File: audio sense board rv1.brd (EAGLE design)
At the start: 127 x 26.7 mm, 33 parts, among them IC2 TSOP38238, J1 PJRAN1X1U01X, J2 PJRAN1X1U01X, Q1 2N3904, Q2 2N3904

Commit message: update lable positions
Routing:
- net IRREC: track 31.3 -> 29.8 mm
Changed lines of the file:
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@@
 <plain>
 <text x="46.228" y="21.717" size="1.397" layer="21" rot="R90">Ch2</text>
-<text x="13.335" y="22.225" size="1.397" layer="21" rot="R270">Ch1</text>
+<text x="14.605" y="20.955" size="1.397" layer="21" rot="R180">Ch1</text>
 <text x="100.33" y="3.048" size="1.016" layer="25">https://github.com/txoof/audioSensor</text>
 <wire x1="0" y1="-1.27" x2="0" y2="25.4" width="0.000253125" layer="20"/>
@@
 </element>
 <element name="IR_LED" library="SparkFun-Connectors" library_urn="urn:adsk.eagle:library:513" package="1X02_LOCK" package3d_urn="urn:adsk.eagle:package:38045/1" value="IR LED connection" x="109.22" y="20.32" smashed="yes" rot="R180">
-<attribute name="NAME" x="114.3" y="18.923" size="0.8128" layer="25" font="vector" ratio="20" rot="R180"/>
+<attribute name="NAME" x="109.22" y="22.733" size="0.8128" layer="25" font="vector" ratio="20" rot="R180"/>
 <attribute name="VALUE" x="110.49" y="22.352" size="0.6096" layer="27" font="vector" ratio="20" rot="R180"/>
 </element>
@@
 </element>
 <element name="DEBUG" library="SparkFun-Connectors" library_urn="urn:adsk.eagle:library:513" package="1X02_LOCK" package3d_urn="urn:adsk.eagle:package:38045/1" value="Debug Jumper" x="121.92" y="20.32" smashed="yes" rot="R180">
-<attribute name="NAME" x="123.19" y="17.907" size="0.8128" layer="25" font="vector" ratio="20"/>
+<attribute name="NAME" x="118.11" y="21.717" size="0.8128" layer="25" font="vector" ratio="20"/>
 <attribute name="VALUE" x="123.19" y="22.352" size="0.6096" layer="27" font="vector" ratio="20" rot="R180"/>
 </element>
@@
 <wire x1="101.6" y1="23.495" x2="101.6" y2="21.77" width="0.3048" layer="16"/>
 <wire x1="123.19" y1="23.495" x2="101.6" y2="23.495" width="0.3048" layer="16"/>
-<wire x1="124.46" y1="22.225" x2="123.19" y2="23.495" width="0.3048" layer="16"/>
-<wire x1="124.46" y1="17.78" x2="124.46" y2="22.225" width="0.3048" layer="16"/>
-<wire x1="123.825" y1="17.145" x2="124.46" y2="17.78" width="0.3048" layer="16"/>
-<wire x1="123.19" y1="17.145" x2="123.825" y2="17.145" width="0.3048" layer="16"/>
-<wire x1="123.19" y1="17.145" x2="123.19" y2="16.97" width="0.3048" layer="16"/>
+<wire x1="123.19" y1="16.97" x2="123.19" y2="23.495" width="0.3048" layer="16"/>
 </signal>
 <signal name="DEBUGJ">

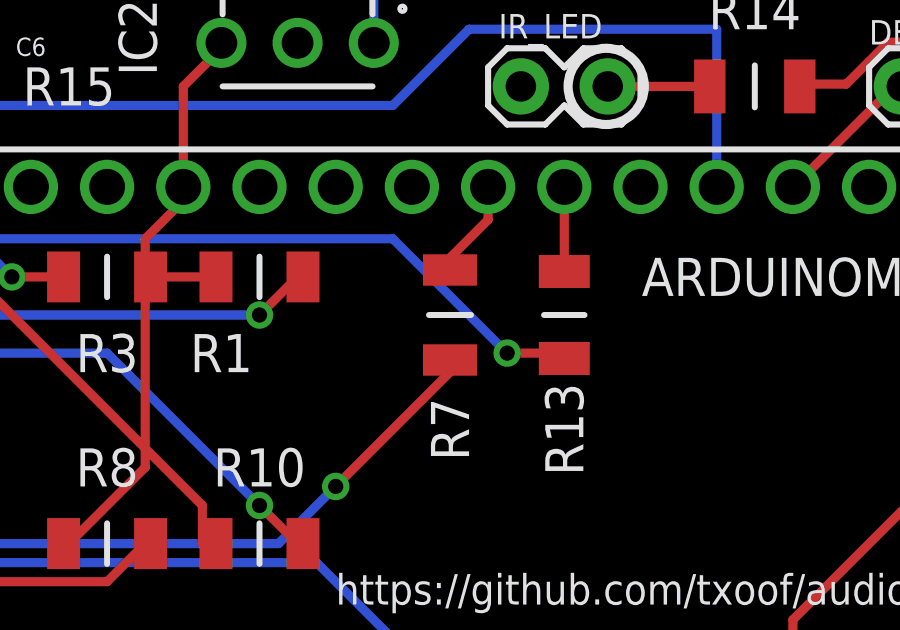
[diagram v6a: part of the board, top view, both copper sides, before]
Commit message: update component values on output LEDs
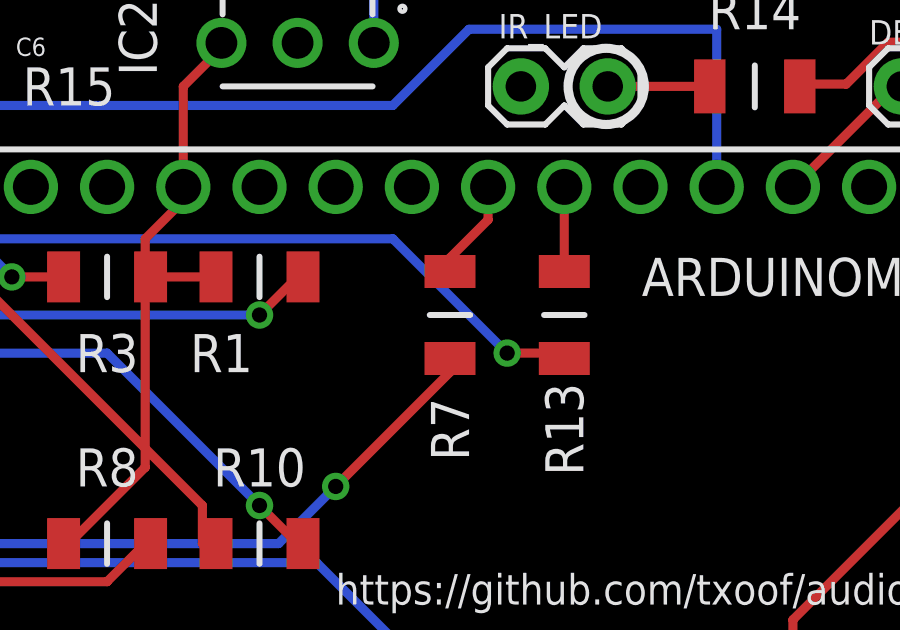
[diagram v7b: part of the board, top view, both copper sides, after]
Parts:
- R13: value ERJ8GEYJ101V -> 100
- R7: value CRCW1206100RJNEAC -> 100; device Samac Populated:RESC3216X60N -> Samac Populated:RESC3116X70N
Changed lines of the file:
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@@
 <drawing>
 <settings>
-<setting alwaysvectorfont="yes"/>
+<setting alwaysvectorfont="no"/>
 <setting verticaltext="up"/>
 </settings>
@@
 <attribute name="VALUE" x="41.91" y="21.59" size="1.27" layer="27" align="center"/>
 </element>
-<element name="R7" library="Samac Populated" package="RESC3216X60N" value="CRCW1206100RJNEAC" x="104.14" y="12.7" smashed="yes" rot="R90">
-<attribute name="DESCRIPTION" value="Thick Film Resistors - SMD 1/4Watt 100ohms 5% Commercial Use" x="104.14" y="12.7" size="1.778" layer="27" rot="R90" display="off"/>
-<attribute name="HEIGHT" value="0.6mm" x="104.14" y="12.7" size="1.778" layer="27" rot="R90" display="off"/>
-<attribute name="MANUFACTURER_NAME" value="Vishay" x="104.14" y="12.7" size="1.778" layer="27" rot="R90" display="off"/>
-<attribute name="MANUFACTURER_PART_NUMBER" value="CRCW1206100RJNEAC" x="104.14" y="12.7" size="1.778" layer="27" rot="R90" display="off"/>
-<attribute name="MOUSER_PART_NUMBER" value="71-CRCW1206100RJNEAC" x="104.14" y="12.7" size="1.778" layer="27" rot="R90" display="off"/>
-<attribute name="MOUSER_PRICE-STOCK" value="https://www.mouser.com/Search/Refine.aspx?Keyword=71-CRCW1206100RJNEAC" x="104.14" y="12.7" size="1.778" layer="27" rot="R90" display="off"/>
+<element name="R7" library="Samac Populated" package="RESC3116X70N" value="100" x="104.14" y="12.7" smashed="yes" rot="R90">
+<attribute name="ALLIED_NUMBER" value="70265175" x="104.14" y="12.7" size="1.778" layer="27" rot="R90" display="off"/>
+<attribute name="ALLIED_PRICE-STOCK" value="https://www.alliedelec.com/panasonic-erj-8geyj101v/70265175/" x="104.14" y="12.7" size="1.778" layer="27" rot="R90" display="off"/>
+<attribute name="DESCRIPTION" value="PANASONIC ELECTRONIC COMPONENTS - ERJ8GEYJ101V - RES, THICK FILM, 100R, 5%, 0.25W, 1206" x="104.14" y="12.7" size="1.778" layer="27" rot="R90" display="off"/>
+<attribute name="HEIGHT" value="0.7mm" x="104.14" y="12.7" size="1.778" layer="27" rot="R90" display="off"/>
+<attribute name="MANUFACTURER_NAME" value="Panasonic" x="104.14" y="12.7" size="1.778" layer="27" rot="R90" display="off"/>
+<attribute name="MANUFACTURER_PART_NUMBER" value="ERJ8GEYJ101V" x="104.14" y="12.7" size="1.778" layer="27" rot="R90" display="off"/>
+<attribute name="MOUSER_PART_NUMBER" value="" x="104.14" y="12.7" size="1.778" layer="27" rot="R90" display="off"/>
+<attribute name="MOUSER_PRICE-STOCK" value="" x="104.14" y="12.7" size="1.778" layer="27" rot="R90" display="off"/>
 <attribute name="NAME" x="104.14" y="8.89" size="1.27" layer="25" rot="R270" align="center"/>
 <attribute name="RS_PART_NUMBER" value="" x="104.14" y="12.7" size="1.778" layer="27" rot="R90" display="off"/>
@@
 <attribute name="VALUE" x="104.14" y="12.7" size="1.27" layer="27" rot="R90" align="center"/>
 </element>
-<element name="R13" library="Samac Populated" package="RESC3116X70N" value="ERJ8GEYJ101V" x="107.95" y="12.7" smashed="yes" rot="R90">
+<element name="R13" library="Samac Populated" package="RESC3116X70N" value="100" x="107.95" y="12.7" smashed="yes" rot="R90">
 <attribute name="ALLIED_NUMBER" value="70265175" x="107.95" y="12.7" size="1.778" layer="27" rot="R90" display="off"/>
 <attribute name="ALLIED_PRICE-STOCK" value="https://www.alliedelec.com/panasonic-erj-8geyj101v/70265175/" x="107.95" y="12.7" size="1.778" layer="27" rot="R90" display="off"/>
@@
 <wire x1="5.715" y1="24.13" x2="9.525" y2="24.13" width="0.3048" layer="1"/>
 <wire x1="5.715" y1="21.59" x2="5.715" y2="24.13" width="0.3048" layer="1"/>
-<wire x1="104.14" y1="10.795" x2="104.14" y2="11.2" width="0.3048" layer="1"/>
+<wire x1="104.14" y1="10.795" x2="104.14" y2="11.25" width="0.3048" layer="1"/>
 <wire x1="5.715" y1="21.59" x2="5.36" y2="21.59" width="0.3048" layer="1"/>
 <via x="100.33" y="6.985" extent="1-16" drill="0.508"/>
@@
 <wire x1="105.41" y1="15.875" x2="104.14" y2="14.605" width="0.3048" layer="1"/>
 <wire x1="105.41" y1="16.97" x2="105.41" y2="15.875" width="0.3048" layer="1"/>
-<wire x1="104.14" y1="14.605" x2="104.14" y2="14.2" width="0.3048" layer="1"/>
+<wire x1="104.14" y1="14.605" x2="104.14" y2="14.15" width="0.3048" layer="1"/>
 </signal>
 <signal name="STATUS_CH2">

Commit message: add holes
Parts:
- moved ARDUINOMICRO 3.81 mm to (86.4, 1.27)
- moved C4 3.81 mm to (53.3, 21.6)
- moved C5 3.81 mm to (53.3, 12.7)
- moved C6 3.81 mm to (90.2, 22.9)
- moved DEBUG 3.81 mm to (125.7, 20.3)
- moved IC2 3.81 mm to (102.9, 20.3)
- moved IR_LED 3.81 mm to (113.0, 20.3)
- moved J2 3.81 mm to (49.5, 2.54)
- moved LED2 3.81 mm to (45.7, 21.6)
- moved Q2 3.81 mm to (45.7, 19.1)
- moved R11 3.81 mm to (53.3, 16.5)
- moved R12 3.81 mm to (87.6, 12.7)
- moved R13 3.81 mm to (111.8, 12.7)
- moved R14 3.81 mm to (118.1, 20.3)
- moved R15 3.81 mm to (90.2, 20.3)
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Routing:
- net IRREC: track 29.8 -> 26.5 mm
- net IRLED: track 33.1 -> 34.4 mm
- net DEBUGJ: track 5.69 -> 5.07 mm
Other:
- board size 127 x 26.7 mm -> 130.8 x 26.7 mm
- board text added: "+"
- board text added: "-"
